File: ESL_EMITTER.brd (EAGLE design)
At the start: 36 x 58 mm, 22 parts, among them IC1 78L05, T1 2N2222, U1 ATTINY85-P

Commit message: feat(labels): add labels & some fix
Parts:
- moved C5 3.16 mm to (10.3, 47.4)
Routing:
- net N$4: track 50.1 -> 53.6 mm
- net N$8: track 12.7 -> 10.1 mm
- net GND: track 122.3 -> 124.7 mm
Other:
- board text added: "100k"
- board text added: "100uF"
- board text added: "10MHz"
- board text added: "10k"
- board text added: "10nF"
- board text added: "220r"
- board text added: "47r"
- board text added: "ATTINY85"
- board text added: "IR LED"

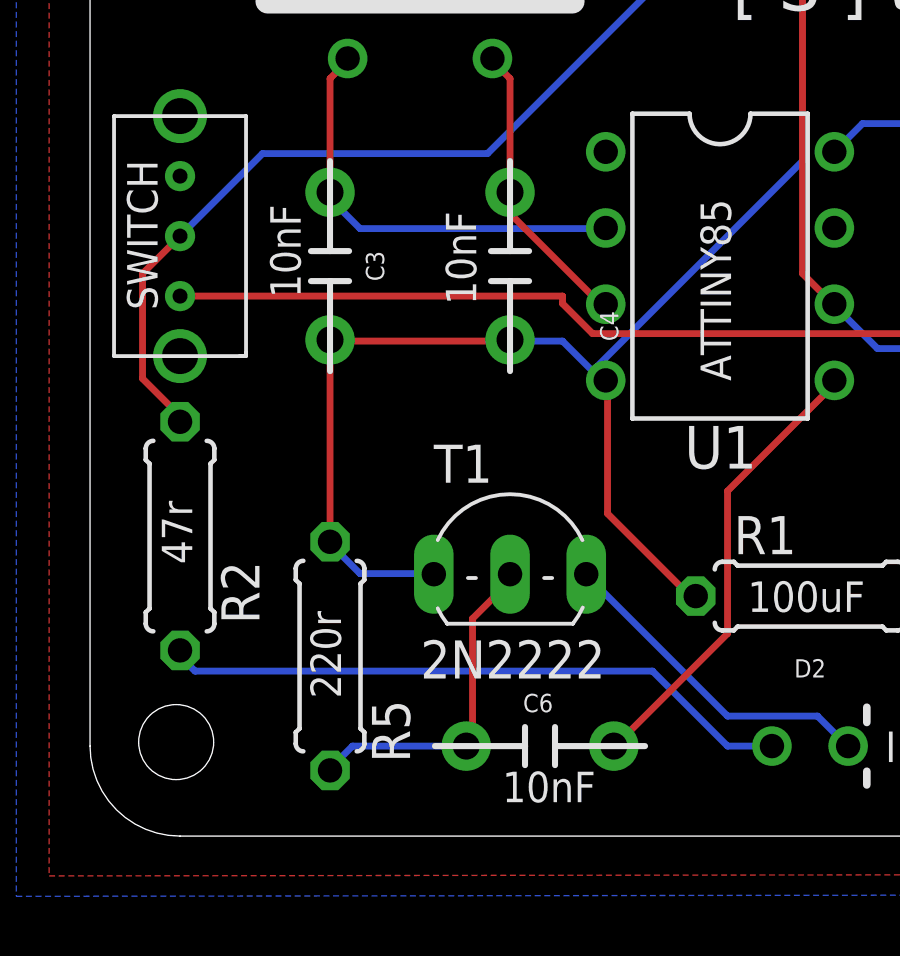
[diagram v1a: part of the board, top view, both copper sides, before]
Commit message: fix: capacitor&bom : last release
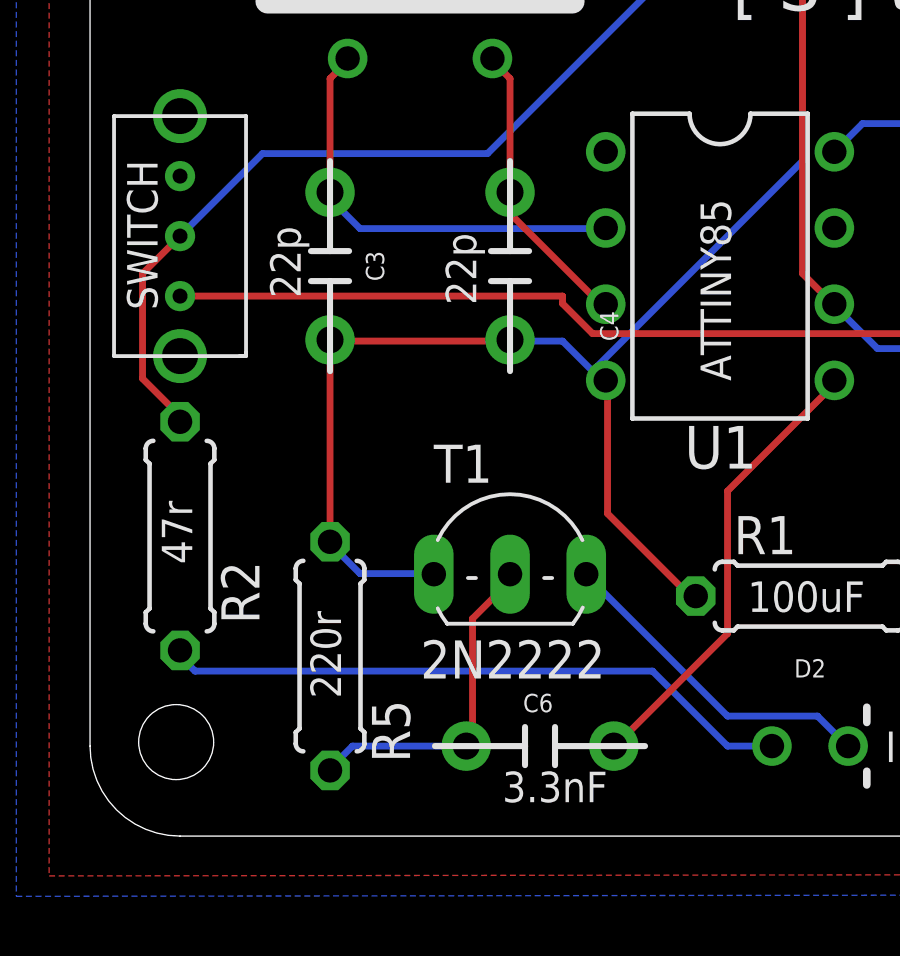
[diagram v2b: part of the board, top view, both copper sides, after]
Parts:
- C3, C4: value 10nF -> 22p
- C6: value 10nF -> 3.3nF
- Q1: value (none) -> 10MHz
- moved FRAME1 21.8 mm to (-0.18, 0.28)
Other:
- board text added: "22p"
- board text added: "3.3nF"
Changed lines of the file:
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@@
 <drawing>
 <settings>
-<setting alwaysvectorfont="yes"/>
+<setting alwaysvectorfont="no"/>
 <setting verticaltext="up"/>
 </settings>
@@
 <text x="21.919165625" y="7.4726875" size="1.016" layer="25">100uF</text>
 <text x="26.5072125" y="2.468103125" size="1.016" layer="25">IR LED</text>
-<text x="13.741559375" y="1.129984375" size="1.016" layer="25">10nF</text>
+<text x="13.741559375" y="1.129984375" size="1.016" layer="25">3.3nF</text>
 <text x="8.365546875" y="4.59230625" size="1.016" layer="25" rot="R90">220r</text>
 <text x="3.4068625" y="9.06499375" size="1.016" layer="25" rot="R90">47r</text>
-<text x="7.022678125" y="17.937815625" size="1.016" layer="25" rot="R90">10nF</text>
-<text x="12.874915625" y="17.71035" size="1.016" layer="25" rot="R90">10nF</text>
+<text x="7.022678125" y="17.937815625" size="1.016" layer="25" rot="R90">22p</text>
+<text x="12.874915625" y="17.71035" size="1.016" layer="25" rot="R90">22p</text>
 <text x="21.367" y="15.174546875" size="1.016" layer="25" rot="R90">ATTINY85</text>
 <text x="7.1049" y="32.442365625" size="1.9304" layer="25">10MHz</text>
@@
 <attribute name="VALUE" x="19.095" y="22.175" size="1.4224" layer="27" ratio="9" rot="R270"/>
 </element>
-<element name="Q1" library="adafruit" package="HC49U-H" value="" x="11" y="31" smashed="yes">
+<element name="Q1" library="adafruit" package="HC49U-H" value="10MHz" x="11" y="31" smashed="yes">
 <attribute name="MF" value="" x="11" y="31" size="1.778" layer="27" display="off"/>
 <attribute name="MPN" value="" x="11" y="31" size="1.778" layer="27" display="off"/>
@@
 <attribute name="VALUE" x="8.46" y="28.968" size="1.27" layer="27" ratio="10" rot="R90"/>
 </element>
-<element name="C3" library="SparkFun-Capacitors" package="CAP-PTH-10MM" value="10nF" x="8" y="19" smashed="yes" rot="R270">
+<element name="C3" library="SparkFun-Capacitors" package="CAP-PTH-10MM" value="22p" x="8" y="19" smashed="yes" rot="R270">
 <attribute name="NAME" x="9.195075" y="19" size="0.6096" layer="25" font="vector" ratio="20" rot="R270" align="bottom-center"/>
 <attribute name="PROD_ID" value="CAP-09321" x="8" y="19" size="1.778" layer="27" rot="R270" display="off"/>
 <attribute name="VALUE" x="7" y="19" size="0.6096" layer="27" font="vector" ratio="20" rot="R270" align="top-center"/>
 </element>
-<element name="C4" library="SparkFun-Capacitors" package="CAP-PTH-10MM" value="10nF" x="14" y="19" smashed="yes" rot="R270">
+<element name="C4" library="SparkFun-Capacitors" package="CAP-PTH-10MM" value="22p" x="14" y="19" smashed="yes" rot="R270">
 <attribute name="NAME" x="17" y="17" size="0.6096" layer="25" font="vector" ratio="20" rot="R270" align="bottom-center"/>
 <attribute name="PROD_ID" value="CAP-09321" x="14" y="19" size="1.778" layer="27" rot="R270" display="off"/>
@@
 <attribute name="VALUE" x="11.46" y="5.428" size="1.27" layer="27" ratio="10"/>
 </element>
-<element name="C6" library="SparkFun-Capacitors" package="CAP-PTH-10MM" value="10nF" x="15" y="3" smashed="yes" rot="R180">
+<element name="C6" library="SparkFun-Capacitors" package="CAP-PTH-10MM" value="3.3nF" x="15" y="3" smashed="yes" rot="R180">
 <attribute name="NAME" x="14.93415" y="4.739996875" size="0.6096" layer="25" font="vector" ratio="20" rot="R180" align="bottom-center"/>
 <attribute name="PROD_ID" value="CAP-09321" x="15" y="3" size="1.778" layer="27" rot="R180" display="off"/>
@@
 <attribute name="VALUE" x="7.4412" y="8.286" size="1.27" layer="27" ratio="10" rot="R270"/>
 </element>
-<element name="FRAME1" library="SparkFun-Retired" package="CREATIVE_COMMONS" value="FRAME-LETTER" x="19" y="-10" smashed="yes"/>
+<element name="FRAME1" library="SparkFun-Retired" package="CREATIVE_COMMONS" value="FRAME-LETTER" x="-0.176940625" y="0.27959375" smashed="yes"/>
 <element name="IN" library="adafruit" package="1X01" value="" x="17" y="56" smashed="yes">
 <attribute name="NAME" x="15.57854375" y="53.054796875" size="1.27" layer="25" ratio="10"/>
